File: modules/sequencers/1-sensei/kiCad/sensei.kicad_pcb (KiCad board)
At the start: 2 copper layers, 150 x 111 mm, 138 parts, among them J1 CLK_IN, J2 CLK OUT, J3 PWR, J4 GATE OUT, J5 CV OUT, J6 GATE_BUS_ENABLE, J7 CV_BUS_ENABLE, J8 CV_LVL_BTM, J9 CV_LVL_TOP, Q1 BC547, Q2 2N3904, Q3 2N3904, Q4 2N3904, Q5 2N3904, Q6 2N3904, Q7 2N3904, Q8 2N3904, Q9 2N3904, U1 TL074, U2 4017

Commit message: add gerber files and ZIPs for V2
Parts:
- H10: renamed from J8; footprint Synth:PinHeader_1x04_P2.54mm_Vertical -> Synth:PinSocket_1x04_P2.54mm_Vertical
- H9: renamed from J9; footprint Synth:PinSocket_1x04_P2.54mm_Vertical -> Synth:PinHeader_1x04_P2.54mm_Vertical
- moved CLK_SPD1 9.00 mm to (135.0, 152.0)
- moved CV_LVL1 9.00 mm to (160.5, 152.0)
- moved D10 9.00 mm to (137.5, 125.0)
- moved D11 9.00 mm to (152.5, 125.0)
- moved D12 9.00 mm to (167.5, 125.0)
- moved D13 9.00 mm to (182.5, 125.0)
- moved D14 9.00 mm to (132.2, 86.0)
- moved D15 9.00 mm to (147.2, 86.0)
- moved D16 9.00 mm to (162.2, 86.0)
- moved D17 9.00 mm to (177.2, 86.0)
- moved D18 9.00 mm to (132.2, 121.0)
- moved D19 9.00 mm to (147.2, 121.0)
- moved D20 9.00 mm to (162.2, 121.0)
- moved D21 9.00 mm to (177.2, 121.0)
- moved D22 9.00 mm to (129.5, 90.0)
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- renumbered H9 to M1, H10 to M2, H11 to M3, H12 to M4, H13 to M5, H14 to M6, H15 to M7, H16 to M8
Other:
- board size 150 x 111 mm -> 141 x 111 mm

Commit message: cleaning up the main readme, update for 3340-vco
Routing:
- added copper zone on F.Cu, net (none)
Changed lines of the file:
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@@
 			)
 		)
-		(model "/Users/lennartquerter/Documents/KiCad/8.0/3dmodels/WQP-PJ398SM.step"
+		(model "/Users/lennart.querter/Documents/KiCad/8.0/3dmodels/WQP-PJ398SM.step"
 			(offset
 				(xyz 0 0 0)
@@
 			(pintype "passive+no_connect")
 		)
-		(model "/Users/lennartquerter/Documents/KiCad/8.0/3dmodels/SPDT-Print-Switch.wrl"
+		(model "/Users/lennart.querter/Documents/KiCad/8.0/3dmodels/SPDT-Print-Switch.wrl"
 			(offset
 				(xyz 0 0 0)
@@
 			(pintype "passive")
 		)
-		(model "/Users/lennartquerter/Documents/KiCad/8.0/3dmodels/P0915N-EC15BR10K.stp"
+		(model "/Users/lennart.querter/Documents/KiCad/8.0/3dmodels/P0915N-EC15BR10K.stp"
 			(offset
 				(xyz 0 0 10)
@@
 			(pintype "passive")
 		)
-		(model "/Users/lennartquerter/Documents/KiCad/8.0/3dmodels/P0915N-EC15BR10K.stp"
+		(model "/Users/lennart.querter/Documents/KiCad/8.0/3dmodels/P0915N-EC15BR10K.stp"
 			(offset
 				(xyz 0 0 10)
@@
 			(pintype "passive+no_connect")
 		)
-		(model "/Users/lennartquerter/Documents/KiCad/8.0/3dmodels/SPDT-Print-Switch.wrl"
+		(model "/Users/lennart.querter/Documents/KiCad/8.0/3dmodels/SPDT-Print-Switch.wrl"
 			(offset
 				(xyz 0 0 0)
@@
 			(pintype "passive")
 		)
-		(model "/Users/lennartquerter/Documents/KiCad/8.0/3dmodels/P0915N-EC15BR10K.stp"
+		(model "/Users/lennart.querter/Documents/KiCad/8.0/3dmodels/P0915N-EC15BR10K.stp"
 			(offset
 				(xyz 0 0 10)
@@
 			)
 		)
-		(model "/Users/lennartquerter/Documents/KiCad/8.0/3dmodels/WQP-PJ398SM.step"
+		(model "/Users/lennart.querter/Documents/KiCad/8.0/3dmodels/WQP-PJ398SM.step"
 			(offset
 				(xyz 0 0 0)
@@
 			(pintype "passive")
 		)
-		(model "/Users/lennartquerter/Documents/KiCad/8.0/3dmodels/SPDT-Print-Switch.wrl"
+		(model "/Users/lennart.querter/Documents/KiCad/8.0/3dmodels/SPDT-Print-Switch.wrl"
 			(offset
 				(xyz 0 0 0)
@@
 			)
 		)
-		(model "/Users/lennartquerter/Documents/KiCad/8.0/3dmodels/WQP-PJ398SM.step"
+		(model "/Users/lennart.querter/Documents/KiCad/8.0/3dmodels/WQP-PJ398SM.step"
 			(offset
 				(xyz 0 0 0)
@@
 			(pintype "passive")
 		)
-		(model "/Users/lennartquerter/Documents/KiCad/8.0/3dmodels/P0915N-EC15BR10K.stp"
+		(model "/Users/lennart.querter/Documents/KiCad/8.0/3dmodels/P0915N-EC15BR10K.stp"
 			(offset
 				(xyz 0 0 10)
@@
 			(pintype "passive+no_connect")
 		)
-		(model "/Users/lennartquerter/Documents/KiCad/8.0/3dmodels/SPDT-Print-Switch.wrl"
+		(model "/Users/lennart.querter/Documents/KiCad/8.0/3dmodels/SPDT-Print-Switch.wrl"
 			(offset
 				(xyz 0 0 0)
@@
 			(pintype "passive+no_connect")
 		)
-		(model "/Users/lennartquerter/Documents/KiCad/8.0/3dmodels/SPDT-Print-Switch.wrl"
+		(model "/Users/lennart.querter/Documents/KiCad/8.0/3dmodels/SPDT-Print-Switch.wrl"
 			(offset
 				(xyz 0 0 0)
@@
 			(pintype "passive")
 		)
-		(model "/Users/lennartquerter/Documents/KiCad/8.0/3dmodels/P0915N-EC15BR10K.stp"
+		(model "/Users/lennart.querter/Documents/KiCad/8.0/3dmodels/P0915N-EC15BR10K.stp"
 			(offset
 				(xyz 0 0 10)
@@
 			(pintype "passive+no_connect")
 		)
-		(model "/Users/lennartquerter/Documents/KiCad/8.0/3dmodels/SPDT-Print-Switch.wrl"
+		(model "/Users/lennart.querter/Documents/KiCad/8.0/3dmodels/SPDT-Print-Switch.wrl"
 			(offset
 				(xyz 0 0 0)
@@
 			(pintype "passive")
 		)
-		(model "/Users/lennartquerter/Documents/KiCad/8.0/3dmodels/P0915N-EC15BR10K.stp"
+		(model "/Users/lennart.querter/Documents/KiCad/8.0/3dmodels/P0915N-EC15BR10K.stp"
 			(offset
 				(xyz 0 0 10)
@@
 			(pintype "passive")
 		)
-		(model "/Users/lennartquerter/Documents/KiCad/8.0/3dmodels/P0915N-EC15BR10K.stp"
+		(model "/Users/lennart.querter/Documents/KiCad/8.0/3dmodels/P0915N-EC15BR10K.stp"
 			(offset
 				(xyz 0 0 10)
@@
 			(pintype "passive")
 		)
-		(model "/Users/lennartquerter/Documents/KiCad/8.0/3dmodels/SPDT-Print-Switch.wrl"
+		(model "/Users/lennart.querter/Documents/KiCad/8.0/3dmodels/SPDT-Print-Switch.wrl"
 			(offset
 				(xyz 0 0 0)
@@
 			(pintype "passive+no_connect")
 		)
-		(model "/Users/lennartquerter/Documents/KiCad/8.0/3dmodels/SPDT-Print-Switch.wrl"
+		(model "/Users/lennart.querter/Documents/KiCad/8.0/3dmodels/SPDT-Print-Switch.wrl"
 			(offset
 				(xyz 0 0 0)
@@
 			(pintype "passive")
 		)
-		(model "/Users/lennartquerter/Documents/KiCad/8.0/3dmodels/P0915N-EC15BR10K.stp"
+		(model "/Users/lennart.querter/Documents/KiCad/8.0/3dmodels/P0915N-EC15BR10K.stp"
 			(offset
 				(xyz 0 0 10)
@@
 			(pintype "passive+no_connect")
 		)
-		(model "/Users/lennartquerter/Documents/KiCad/8.0/3dmodels/SPDT-Print-Switch.wrl"
+		(model "/Users/lennart.querter/Documents/KiCad/8.0/3dmodels/SPDT-Print-Switch.wrl"
 			(offset
 				(xyz 0 0 0)
@@
 			(pintype "passive")
 		)
-		(model "/Users/lennartquerter/Documents/KiCad/8.0/3dmodels/P0915N-EC15BR10K.stp"
+		(model "/Users/lennart.querter/Documents/KiCad/8.0/3dmodels/P0915N-EC15BR10K.stp"
 			(offset
 				(xyz 0 0 10)
@@
 			(pintype "passive+no_connect")
 		)
-		(model "/Users/lennartquerter/Documents/KiCad/8.0/3dmodels/SPDT-Print-Switch.wrl"
+		(model "/Users/lennart.querter/Documents/KiCad/8.0/3dmodels/SPDT-Print-Switch.wrl"
 			(offset
 				(xyz 0 0 0)
@@
 			)
 		)
-		(model "/Users/lennartquerter/Documents/KiCad/8.0/3dmodels/WQP-PJ398SM.step"
+		(model "/Users/lennart.querter/Documents/KiCad/8.0/3dmodels/WQP-PJ398SM.step"
 			(offset
 				(xyz 0 0 0)
@@
 	)
 	(zone
+		(net 0)
+		(net_name "")
+		(layer "F.Cu")
+		(hatch edge 0.5)
+		(priority 1)
+		(connect_pads
+			(clearance 0.5)
+		)
+		(min_thickness 0.25)
+		(filled_areas_thickness no)
+		(fill yes
+			(thermal_gap 0.5)
+			(thermal_bridge_width 0.5)
+			(island_removal_mode 1)
+			(island_area_min 10)
+		)
+		(polygon
+			(pts
+				(xy 45 45) (xy 195 45) (xy 195 165) (xy 45 165)
+			)
+		)
+	)
+	(zone

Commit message: final versions of PCB for modules
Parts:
- moved M4 2.50 mm to (55.0, 140.0)
- moved H17 1.36 mm to (188.0, 64.0)
- moved H18 1.28 mm to (117.0, 64.0)
- moved M1 0.24 mm to (65.0, 54.0)
- moved RV5 0.08 mm to (133.5, 100.0)
- moved RV6 0.08 mm to (148.5, 100.0)
- moved RV7 0.08 mm to (163.5, 100.0)
- moved RV8 0.08 mm to (178.5, 100.0)
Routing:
- net +12V: track 290.7 -> 286.8 mm
- net Net-(H4D-Pin_4): track 42.8 -> 40.6 mm
- net Net-(H4B-Pin_2): track 30.0 -> 31.5 mm
- net Net-(H4C-Pin_3): track 19.0 -> 18.4 mm

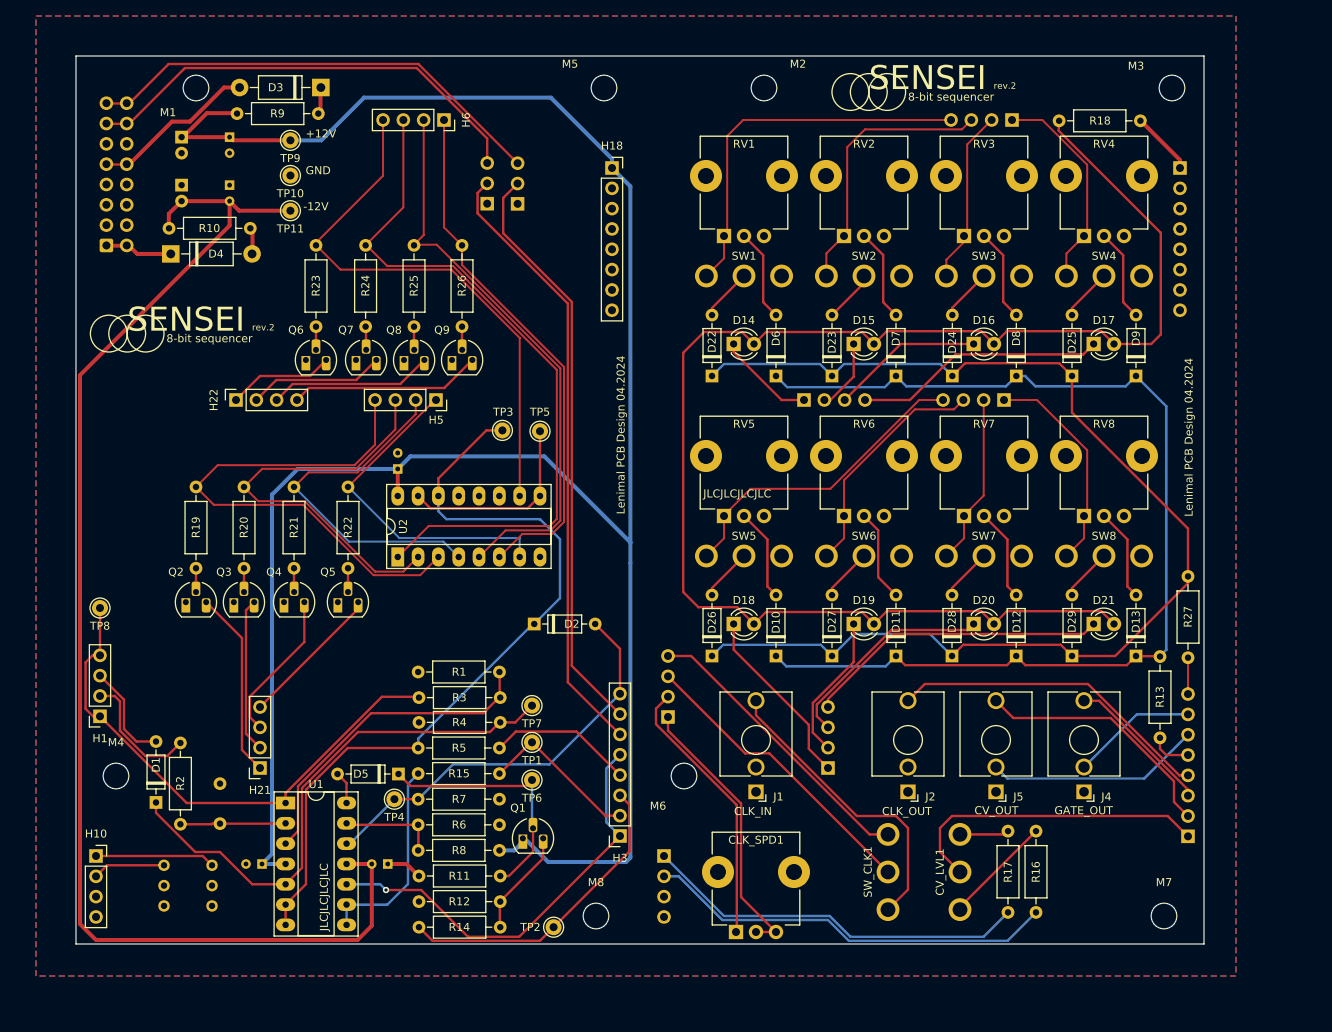
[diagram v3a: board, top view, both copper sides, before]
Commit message: update to BOM and add panels
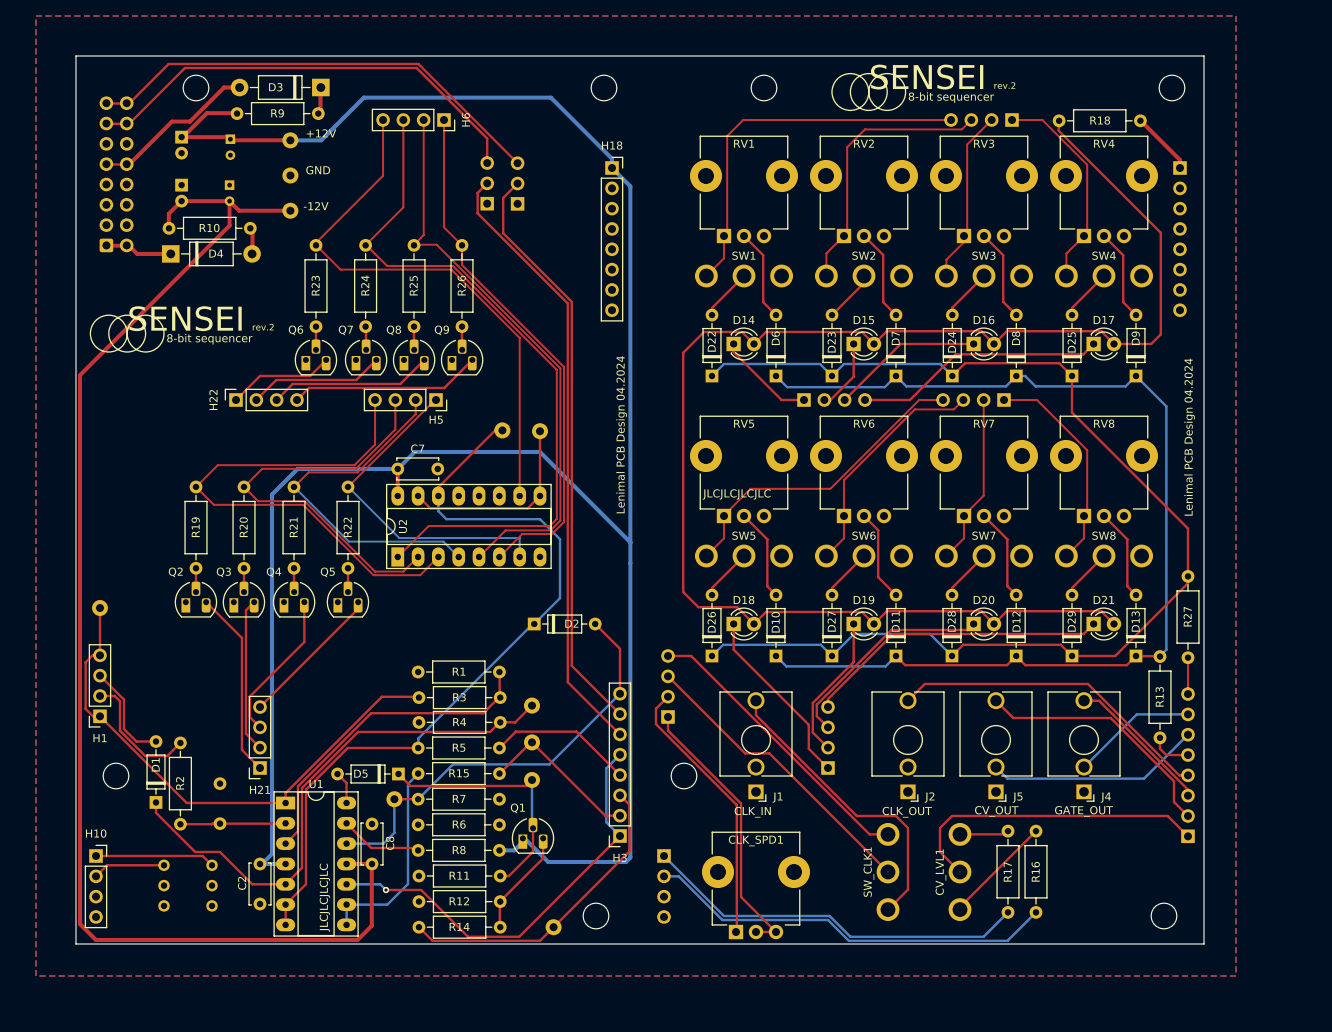
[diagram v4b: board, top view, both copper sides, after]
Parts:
- C1: value 0.1 uF -> 1uF
- C2, C7, C8: footprint Capacitor_THT:CP_Radial_D4.0mm_P2.00mm -> Capacitor_THT:C_Disc_D5.0mm_W2.5mm_P5.00mm; moved to F.Cu
- H1: value BTM_CLK -> PinSocket_1x04
- H10: value CV_LVL_BTM -> PinSocket_1x04
- H17: value TOP_PWR -> PinHeader_1x08
- H18: value BTM_PWR -> PinSocket_1x08
- H19: value TOP_LED_RW_1 -> PinHeader_1x04
- H2: value TOP_CLK -> PinHeader_1x04
- H20: value TOP_LED_RW_2 -> PinHeader_1x04
- H21: value BTM_LED_RW_1 -> PinSocket_1x04
- H22: value BTM_LED_RW_2 -> PinSocket_1x04
- H3: value BTM_CTRL -> PinSocket_1x08
- H4: value TOP_CTRL -> PinHeader_1x08
- H5: value BTM_SGL_RW_2 -> PinSocket_1x04
- H6: value BTM_SGL_RW_1 -> PinSocket_1x04
- H7: value TOP_SGL_RW_2 -> PinHeader_1x04
- H8: value TOP_SGL_RW_1 -> PinHeader_1x04
- H9: value CV_LVL_TOP -> PinHeader_1x04
- J6: value GATE_BUS_ENABLE -> PinHeader_1x03
- J7: value CV_BUS_ENABLE -> PinHeader_1x03
- R10, R9: value 10 -> 10R
- R14: value 200 -> 200R
- R18: value 1K -> 470R
- TP1, TP10, TP11, TP2, TP3, TP4, TP5, TP6, TP7, TP8, TP9: moved to B.Cu
- U2: value 4017 -> CD4017
- moved C2 90.9 mm to (73.0, 151.0)
- moved C5 90.7 mm to (69.3, 60.4), turned to -90 degrees
- moved C8 5.38 mm to (87.0, 146.0), turned to -90 degrees
- turned C7 to 0 degrees
- turned TP1 to 180 degrees
- turned TP10 to 180 degrees
- turned TP11 to 180 degrees
- turned TP2 to 180 degrees
- turned TP3 to 180 degrees
- turned TP4 to 180 degrees
- turned TP5 to 180 degrees
- turned TP6 to 180 degrees
- turned TP7 to 180 degrees
- turned TP8 to 180 degrees
- turned TP9 to 180 degrees
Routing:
- net GNDREF: track 4.47 -> 0.00 mm
- net Net-(D2-A): track 52.0 -> 54.4 mm
- net Net-(U1D--): track 12.3 -> 10.4 mm
- net Net-(D2-K): track 98.9 -> 98.3 mm
